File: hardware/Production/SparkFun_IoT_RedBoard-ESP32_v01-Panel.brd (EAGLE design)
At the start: 246.1 x 248.9 mm, 2514 parts, among them J1 5.5x2.1mm Barrel, J101 USB C, J102 USB_SOLDER_PADS, J103 M10NO_SILK, J108 QWIIC_RIGHT_ANGLE, J109 MICRO-SD-PUSH-PUSH-EXT-PIN, J110 5.5x2.1mm Barrel, J117 USB C, J118 USB_SOLDER_PADS, J119 M10NO_SILK, J124 QWIIC_RIGHT_ANGLE, J125 MICRO-SD-PUSH-PUSH-EXT-PIN, J126 5.5x2.1mm Barrel, J13 QWIIC_RIGHT_ANGLE, J133 USB C, J134 USB_SOLDER_PADS, J135 M10NO_SILK, J140 QWIIC_RIGHT_ANGLE, J141 MICRO-SD-PUSH-PUSH-EXT-PIN, J142 5.5x2.1mm Barrel, J149 USB C, J15 MICRO-SD-PUSH-PUSH-EXT-PIN, J150 USB_SOLDER_PADS, J151 M10NO_SILK, J156 QWIIC_RIGHT_ANGLE, J157 MICRO-SD-PUSH-PUSH-EXT-PIN, J158 5.5x2.1mm Barrel, J165 USB C, J166 USB_SOLDER_PADS, J167 M10NO_SILK, J172 QWIIC_RIGHT_ANGLE, J173 MICRO-SD-PUSH-PUSH-EXT-PIN, J174 5.5x2.1mm Barrel, J181 USB C, J182 USB_SOLDER_PADS, J183 M10NO_SILK, J188 QWIIC_RIGHT_ANGLE, J189 MICRO-SD-PUSH-PUSH-EXT-PIN, J190 5.5x2.1mm Barrel, J2 USB C, J21 USB C, J22 USB_SOLDER_PADS, J23 M10NO_SILK, J28 QWIIC_RIGHT_ANGLE, J29 MICRO-SD-PUSH-PUSH-EXT-PIN, J3 USB_SOLDER_PADS, J30 5.5x2.1mm Barrel, J37 USB C, J38 USB_SOLDER_PADS, J39 M10NO_SILK, J44 QWIIC_RIGHT_ANGLE, J45 MICRO-SD-PUSH-PUSH-EXT-PIN, J46 5.5x2.1mm Barrel, J5 M10NO_SILK, J53 USB C, J54 USB_SOLDER_PADS, J55 M10NO_SILK, J60 QWIIC_RIGHT_ANGLE, J61 MICRO-SD-PUSH-PUSH-EXT-PIN, J62 5.5x2.1mm Barrel, J69 USB C, J70 USB_SOLDER_PADS, J71 M10NO_SILK, J76 QWIIC_RIGHT_ANGLE, J77 MICRO-SD-PUSH-PUSH-EXT-PIN, J78 5.5x2.1mm Barrel, J85 USB C, J86 USB_SOLDER_PADS, J87 M10NO_SILK, J92 QWIIC_RIGHT_ANGLE, J93 MICRO-SD-PUSH-PUSH-EXT-PIN, J94 5.5x2.1mm Barrel, Q1 MBT3904DW1T1, Q100 20V/4.2A/52mΩ/1.4W, Q102 20V/4.2A/52mΩ/1.4W, Q104 20V/4.2A/52mΩ/1.4W, Q105 MBT3904DW1T1, Q107 20V/4.2A/52mΩ/1.4W, Q109 20V/4.2A/52mΩ/1.4W, Q11 20V/4.2A/52mΩ/1.4W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

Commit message: Implemented changes suggested by Pete Lewis.
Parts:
- removed LOGO49, LOGO52, LOGO54, LOGO57, LOGO59: QWIIC_LOGO_5MM, SparkFun-Aesthetics:QWIIC_5MM
- removed LOGO50, LOGO55, LOGO60: SFE_LOGO_NAME_FLAME.2_INCH, SparkFun-Aesthetics:SFE_LOGO_NAME_FLAME_.2
- removed LOGO51, LOGO56: SFE_LOGO_NAME.1_INCH, SparkFun-Aesthetics:SFE_LOGO_NAME_.1
- removed LOGO53, LOGO58: OSHW-LOGOMINI, SparkFun-Aesthetics:OSHW-LOGO-MINI
- added U$1177: (no value), output-ESP32:#3#3V#321866
- added U$1178: (no value), output-ESP32:#MEAS#1851
- added U$1179: (no value), output-ESP32:#BYP#35
- added U$1180: (no value), output-ESP32:D#32321863
- added U$1181: (no value), output-ESP32:D#32321862
- added U$1182: (no value), output-ESP32:G32321864
- added U$1183: (no value), output-ESP32:#1849
- added U$1184: (no value), output-ESP32:#1850
- added U$1185: (no value), output-ESP32:#I2C#1855
- added U$1186: (no value), output-ESP32:##ALERT##1852
- added U$1187: (no value), output-ESP32:#TMS#1854
- added U$1188: (no value), output-ESP32:#TCK#1853
- added U$1189, U$1190: (no value), output-ESP32:INPUT_ONLY321867
- added U$1191: (no value), output-ESP32:##ALERT##4#321866
- added U$1192: (no value), output-ESP32:TP1321868
- added U$1193: (no value), SparkFun-Aesthetics:REDBOARD_LOGO
- added U$1194: (no value), output-ESP32:#IOT#132321869
- added U$1195: (no value), output-ESP32:ESP32321856
- added U$1196: (no value), output-ESP32:#IOT#132321874
- added U$1197: (no value), output-ESP32:MADE_IN32321857
- added U$1198: (no value), output-ESP32:THE_USA32321858
- added U$1199: (no value), output-ESP32:7#15V32321861
- added U$1200: (no value), output-ESP32:3#3V_LOGIC_SHIELDS_ONLY132321876
- LOGO10, LOGO30: value SFE_LOGO_NAME_FLAME.2_INCH -> QWIIC_LOGO_5MM; device SparkFun-Aesthetics:SFE_LOGO_NAME_FLAME_.2 -> SparkFun-Aesthetics:QWIIC_5MM
- LOGO11, LOGO31: value SFE_LOGO_NAME.1_INCH -> OSHW-LOGOMINI; device SparkFun-Aesthetics:SFE_LOGO_NAME_.1 -> SparkFun-Aesthetics:OSHW-LOGO-MINI
- LOGO12, LOGO24, LOGO32, LOGO44: value QWIIC_LOGO_5MM -> SFE_LOGO_NAME_FLAME.2_INCH; device SparkFun-Aesthetics:QWIIC_5MM -> SparkFun-Aesthetics:SFE_LOGO_NAME_FLAME_.2
- LOGO13, LOGO33: value OSHW-LOGOMINI -> SFE_LOGO_NAME.1_INCH; device SparkFun-Aesthetics:OSHW-LOGO-MINI -> SparkFun-Aesthetics:SFE_LOGO_NAME_.1
- LOGO15, LOGO35: value SFE_LOGO_NAME_FLAME.2_INCH -> OSHW-LOGOMINI; device SparkFun-Aesthetics:SFE_LOGO_NAME_FLAME_.2 -> SparkFun-Aesthetics:OSHW-LOGO-MINI
- LOGO16, LOGO36: value SFE_LOGO_NAME.1_INCH -> SFE_LOGO_NAME_FLAME.2_INCH; device SparkFun-Aesthetics:SFE_LOGO_NAME_.1 -> SparkFun-Aesthetics:SFE_LOGO_NAME_FLAME_.2
- LOGO17, LOGO29, LOGO37, LOGO4, LOGO9: value QWIIC_LOGO_5MM -> SFE_LOGO_NAME.1_INCH; device SparkFun-Aesthetics:QWIIC_5MM -> SparkFun-Aesthetics:SFE_LOGO_NAME_.1
- LOGO18, LOGO38: value OSHW-LOGOMINI -> QWIIC_LOGO_5MM; device SparkFun-Aesthetics:OSHW-LOGO-MINI -> SparkFun-Aesthetics:QWIIC_5MM
- LOGO19, LOGO27, LOGO39, LOGO47, LOGO7: value QWIIC_LOGO_5MM -> OSHW-LOGOMINI; device SparkFun-Aesthetics:QWIIC_5MM -> SparkFun-Aesthetics:OSHW-LOGO-MINI
- LOGO25, LOGO45: value SFE_LOGO_NAME_FLAME.2_INCH -> SFE_LOGO_NAME.1_INCH; device SparkFun-Aesthetics:SFE_LOGO_NAME_FLAME_.2 -> SparkFun-Aesthetics:SFE_LOGO_NAME_.1
- LOGO26, LOGO46, LOGO5: value SFE_LOGO_NAME.1_INCH -> QWIIC_LOGO_5MM; device SparkFun-Aesthetics:SFE_LOGO_NAME_.1 -> SparkFun-Aesthetics:QWIIC_5MM
- LOGO28, LOGO48, LOGO8: value OSHW-LOGOMINI -> SFE_LOGO_NAME_FLAME.2_INCH; device SparkFun-Aesthetics:OSHW-LOGO-MINI -> SparkFun-Aesthetics:SFE_LOGO_NAME_FLAME_.2
- U$1000: device output-ESP32:#14#14 -> output-ESP32:3#3V_LOGIC_SHIELDS_ONLY132321876
- U$1001: device output-ESP32:#13#5 -> output-ESP32:V323252
- U$1002: device output-ESP32:#4#2 -> output-ESP32:#SCL#34
- U$1003: device output-ESP32:#TX#O#0 -> output-ESP32:#SDA#33
- U$1004: device output-ESP32:#RX#I#1 -> output-ESP32:#3#3V#33
- U$1005: device output-ESP32:#RESET#1842 -> output-ESP32:#GND#32
- U$1006: device output-ESP32:#BOOT#1841 -> output-ESP32:#SCK#31
- U$1007: device output-ESP32:#JTAG#1847 -> output-ESP32:#POCI#30
- U$1008: device output-ESP32:#A0#1843 -> output-ESP32:#PICO#29
- U$1009: device output-ESP32:#A3#1843 -> output-ESP32:1836
- U$101, U$199: device output-ESP32:#SDA#33 -> output-ESP32:7#15V32321861
- U$1010: device output-ESP32:#A6#1843 -> output-ESP32:##CS##28
- U$1011: device output-ESP32:#A7#1843 -> output-ESP32:#27#27
- U$1012: device output-ESP32:#A4#1843 -> output-ESP32:#26#26
- U$1013: device output-ESP32:#A5#1843 -> output-ESP32:TX1838
- U$1014: device output-ESP32:#VIN#1843 -> output-ESP32:RX1839
- U$1015: device output-ESP32:#GND#1844 -> output-ESP32:PWR1837
- U$1016: device output-ESP32:#GND#1844 -> output-ESP32:CHG1840
- U$1017: device output-ESP32:#5V#1845 -> output-ESP32:#25#18
- U$1018: device output-ESP32:#3#3V#1845 -> output-ESP32:#17#17
- U$1019: device output-ESP32:##RST##1845 -> output-ESP32:#16#15
- U$102: device output-ESP32:#3#3V#33 -> output-ESP32:#SDA#33
- U$1020: device output-ESP32:#REF#1846 -> output-ESP32:#14#14
- U$1021: device output-ESP32:#MEAS#1851 -> output-ESP32:#13#5
- U$1022: device output-ESP32:#1849 -> output-ESP32:#4#2
- U$1023: device output-ESP32:#1850 -> output-ESP32:#TX#O#0
- U$1024: device output-ESP32:#BATT#1848 -> output-ESP32:#RX#I#1
- U$1025, U$125: device output-ESP32:#JTAG#1847 -> output-ESP32:#RESET#1842
- U$1026: device output-ESP32:ESP321855 -> output-ESP32:#BOOT#1841
- U$1027, U$145: device output-ESP32:7#15V32321861 -> output-ESP32:#JTAG#1847
- U$1028: device output-ESP32:#39#A3#321862 -> output-ESP32:#A0#1843
- U$1029: device output-ESP32:#36#A0#321862 -> output-ESP32:#A3#1843
- U$103: device output-ESP32:#GND#32 -> output-ESP32:3#3V_LOGIC_SHIELDS_ONLY132321876
- U$1030: device output-ESP32:#34#A6#32321865 -> output-ESP32:#A6#1843
- U$1031: device output-ESP32:#35#A7#321862 -> output-ESP32:#A7#1843
- U$1032: device output-ESP32:#32#A4#32321865 -> output-ESP32:#A4#1843
- U$1033: device output-ESP32:#34#A6#321862 -> output-ESP32:#A5#1843
- U$1034: device output-ESP32:#VIN#321862 -> output-ESP32:#VIN#1843
- U$1035, U$1136: device output-ESP32:#GND#321863 -> output-ESP32:#GND#1844
- U$1036: device output-ESP32:#5V#321864 -> output-ESP32:#GND#1844
- U$1037: device output-ESP32:#3#3V#321864 -> output-ESP32:#5V#1845
- U$1038: device output-ESP32:#GND#321863 -> output-ESP32:#3#3V#1845
- U$1039: device output-ESP32:##RESET##321864 -> output-ESP32:##RST##1845
- U$104: device output-ESP32:#SCK#31 -> output-ESP32:#3#3V#33
- U$1040: device output-ESP32:#IOREF#321865 -> output-ESP32:#REF#1846
- U$1041: device output-ESP32:#3#RX#I#32321869 -> output-ESP32:#MEAS#1851
- U$1042: device output-ESP32:#1#TX#O#32321869 -> output-ESP32:#1849
- U$1043: device output-ESP32:#13#TCK#32321869 -> output-ESP32:#1850
- U$1044: device output-ESP32:#14#TMS#32321869 -> output-ESP32:#BATT#1848
- U$1045: device output-ESP32:#16#32321869 -> output-ESP32:#JTAG#1847
- U$1046: device output-ESP32:#17#32321869 -> output-ESP32:ESP321855
- U$1047: device output-ESP32:#25#32321869 -> output-ESP32:7#15V32321861
- U$1048: device output-ESP32:#26#32321869 -> output-ESP32:#39#A3#321862
- U$1049: device output-ESP32:#5##CS##32321869 -> output-ESP32:#36#A0#321862
- U$105: device output-ESP32:#POCI#30 -> output-ESP32:#GND#32
- U$1050: device output-ESP32:#23#PICO#321866 -> output-ESP32:#34#A6#32321865
- U$1051: device output-ESP32:#19#POCI#321866 -> output-ESP32:#35#A7#321862
- U$1052: device output-ESP32:#18#SCK#32321869 -> output-ESP32:#32#A4#32321865
- U$1053: device output-ESP32:#21#SDA#32321869 -> output-ESP32:#34#A6#321862
- U$1054: device output-ESP32:#22#SCL#32321869 -> output-ESP32:#VIN#321862
- U$1055: device output-ESP32:#27#32321869 -> output-ESP32:#GND#321863
- U$1056: device output-ESP32:#GND#321866 -> output-ESP32:#5V#321864
- U$1057: device output-ESP32:#3#3V#321866 -> output-ESP32:#3#3V#321864
- U$1058: device output-ESP32:#MEAS#1851 -> output-ESP32:#GND#321863
- U$1059: device output-ESP32:#BYP#35 -> output-ESP32:##RESET##321864
- U$106: device output-ESP32:#PICO#29 -> output-ESP32:#SCK#31
- U$1060: device output-ESP32:D#32321863 -> output-ESP32:#IOREF#321865
- U$1061: device output-ESP32:D#32321862 -> output-ESP32:#3#RX#I#32321869
- U$1062: device output-ESP32:G32321864 -> output-ESP32:#1#TX#O#32321869
- U$1063: device output-ESP32:#1849 -> output-ESP32:#13#TCK#32321869
- U$1064: device output-ESP32:#1850 -> output-ESP32:#14#TMS#32321869
- U$1065: device output-ESP32:#I2C#1855 -> output-ESP32:#16#32321869
- U$1066: device output-ESP32:##ALERT##1852 -> output-ESP32:#17#32321869
- U$1067: device output-ESP32:#TMS#1854 -> output-ESP32:#25#32321869
- U$1068: device output-ESP32:#TCK#1853 -> output-ESP32:#26#32321869
- U$1069: device output-ESP32:INPUT_ONLY321867 -> output-ESP32:#5##CS##32321869
- U$107: device output-ESP32:1836 -> output-ESP32:#POCI#30
- U$1070: device output-ESP32:INPUT_ONLY321867 -> output-ESP32:#23#PICO#321866
- U$1071: device output-ESP32:##ALERT##4#321866 -> output-ESP32:#19#POCI#321866
- U$1072: device output-ESP32:TP1321868 -> output-ESP32:#18#SCK#32321869
- U$1073: device SparkFun-Aesthetics:REDBOARD_LOGO -> output-ESP32:#21#SDA#32321869
- U$1074: device output-ESP32:#IOT#132321869 -> output-ESP32:#22#SCL#32321869
- U$1075: device output-ESP32:ESP32321856 -> output-ESP32:#27#32321869
- U$1076: device output-ESP32:#IOT#132321874 -> output-ESP32:#GND#321866
- U$1077: device output-ESP32:MADE_IN32321857 -> output-ESP32:#3#3V#321866
- U$1078: device output-ESP32:THE_USA32321858 -> output-ESP32:#MEAS#1851
- U$1079: device output-ESP32:V323252 -> output-ESP32:#BYP#35
- U$108: device output-ESP32:##CS##28 -> output-ESP32:#PICO#29
- U$1080: device output-ESP32:#SCL#34 -> output-ESP32:D#32321863
- U$1081: device output-ESP32:#SDA#33 -> output-ESP32:D#32321862
- U$1082: device output-ESP32:#3#3V#33 -> output-ESP32:G32321864
- U$1083: device output-ESP32:#GND#32 -> output-ESP32:#1849
- U$1084: device output-ESP32:#SCK#31 -> output-ESP32:#1850
- U$1085: device output-ESP32:#POCI#30 -> output-ESP32:#I2C#1855
- U$1086: device output-ESP32:#PICO#29 -> output-ESP32:##ALERT##1852
- U$1087: device output-ESP32:1836 -> output-ESP32:#TMS#1854
- U$1088: device output-ESP32:##CS##28 -> output-ESP32:#TCK#1853
- U$1089: device output-ESP32:#27#27 -> output-ESP32:INPUT_ONLY321867
- U$109: device output-ESP32:#27#27 -> output-ESP32:1836
- U$1090: device output-ESP32:#26#26 -> output-ESP32:INPUT_ONLY321867
- U$1091: device output-ESP32:TX1838 -> output-ESP32:##ALERT##4#321866
- U$1092: device output-ESP32:RX1839 -> output-ESP32:TP1321868
- U$1093: device output-ESP32:PWR1837 -> SparkFun-Aesthetics:REDBOARD_LOGO
- U$1094: device output-ESP32:CHG1840 -> output-ESP32:#IOT#132321869
- U$1095: device output-ESP32:#25#18 -> output-ESP32:ESP32321856
- U$1096: device output-ESP32:#17#17 -> output-ESP32:#IOT#132321874
- U$1097: device output-ESP32:#16#15 -> output-ESP32:MADE_IN32321857
- U$1098: device output-ESP32:#14#14 -> output-ESP32:THE_USA32321858
- U$1099: device output-ESP32:#13#5 -> output-ESP32:7#15V32321861
- U$110: device output-ESP32:#26#26 -> output-ESP32:##CS##28
- U$1100: device output-ESP32:#4#2 -> output-ESP32:3#3V_LOGIC_SHIELDS_ONLY132321876
- U$1101: device output-ESP32:#TX#O#0 -> output-ESP32:V323252
- U$1102: device output-ESP32:#RX#I#1 -> output-ESP32:#SCL#34
- U$1103: device output-ESP32:#RESET#1842 -> output-ESP32:#SDA#33
- U$1104: device output-ESP32:#BOOT#1841 -> output-ESP32:#3#3V#33
- U$1105: device output-ESP32:#JTAG#1847 -> output-ESP32:#GND#32
- U$1106: device output-ESP32:#A0#1843 -> output-ESP32:#SCK#31
- U$1107: device output-ESP32:#A3#1843 -> output-ESP32:#POCI#30
- U$1108: device output-ESP32:#A6#1843 -> output-ESP32:#PICO#29
- U$1109: device output-ESP32:#A7#1843 -> output-ESP32:1836
- U$111: device output-ESP32:TX1838 -> output-ESP32:#27#27
- U$1110: device output-ESP32:#A4#1843 -> output-ESP32:##CS##28
- U$1111: device output-ESP32:#A5#1843 -> output-ESP32:#27#27
- U$1112: device output-ESP32:#VIN#1843 -> output-ESP32:#26#26
- U$1113: device output-ESP32:#GND#1844 -> output-ESP32:TX1838
- U$1114: device output-ESP32:#GND#1844 -> output-ESP32:RX1839
- U$1115: device output-ESP32:#5V#1845 -> output-ESP32:PWR1837
- U$1116: device output-ESP32:#3#3V#1845 -> output-ESP32:CHG1840
- U$1117: device output-ESP32:##RST##1845 -> output-ESP32:#25#18
- U$1118: device output-ESP32:#REF#1846 -> output-ESP32:#17#17
- U$1119: device output-ESP32:#MEAS#1851 -> output-ESP32:#16#15
- U$112: device output-ESP32:RX1839 -> output-ESP32:#26#26
- U$1120: device output-ESP32:#1849 -> output-ESP32:#14#14
- U$1121: device output-ESP32:#1850 -> output-ESP32:#13#5
- U$1122: device output-ESP32:#BATT#1848 -> output-ESP32:#4#2
- U$1123, U$223: device output-ESP32:#JTAG#1847 -> output-ESP32:#TX#O#0
- U$1124: device output-ESP32:ESP321855 -> output-ESP32:#RX#I#1
- U$1125: device output-ESP32:7#15V32321861 -> output-ESP32:#RESET#1842
- U$1126: device output-ESP32:#39#A3#321862 -> output-ESP32:#BOOT#1841
- U$1127, U$245: device output-ESP32:#36#A0#321862 -> output-ESP32:#JTAG#1847
- U$1128: device output-ESP32:#34#A6#32321865 -> output-ESP32:#A0#1843
- U$1129: device output-ESP32:#35#A7#321862 -> output-ESP32:#A3#1843
- U$113: device output-ESP32:PWR1837 -> output-ESP32:TX1838
- U$1130: device output-ESP32:#32#A4#32321865 -> output-ESP32:#A6#1843
- U$1131: device output-ESP32:#34#A6#321862 -> output-ESP32:#A7#1843
- U$1132: device output-ESP32:#VIN#321862 -> output-ESP32:#A4#1843
- U$1133: device output-ESP32:#GND#321863 -> output-ESP32:#A5#1843
- U$1134: device output-ESP32:#5V#321864 -> output-ESP32:#VIN#1843
- U$1135: device output-ESP32:#3#3V#321864 -> output-ESP32:#GND#1844
- U$1137: device output-ESP32:##RESET##321864 -> output-ESP32:#5V#1845
- U$1138: device output-ESP32:#IOREF#321865 -> output-ESP32:#3#3V#1845
- U$1139: device output-ESP32:#3#RX#I#32321869 -> output-ESP32:##RST##1845
- U$114: device output-ESP32:CHG1840 -> output-ESP32:RX1839
- U$1140: device output-ESP32:#1#TX#O#32321869 -> output-ESP32:#REF#1846
- U$1141: device output-ESP32:#13#TCK#32321869 -> output-ESP32:#MEAS#1851
- U$1142: device output-ESP32:#14#TMS#32321869 -> output-ESP32:#1849
- U$1143: device output-ESP32:#16#32321869 -> output-ESP32:#1850
- U$1144: device output-ESP32:#17#32321869 -> output-ESP32:#BATT#1848
- U$1145: device output-ESP32:#25#32321869 -> output-ESP32:#JTAG#1847
- U$1146: device output-ESP32:#26#32321869 -> output-ESP32:ESP321855
- U$1147: device output-ESP32:#5##CS##32321869 -> output-ESP32:7#15V32321861
- U$1148: device output-ESP32:#23#PICO#321866 -> output-ESP32:#39#A3#321862
- U$1149: device output-ESP32:#19#POCI#321866 -> output-ESP32:#36#A0#321862
- U$115: device output-ESP32:#25#18 -> output-ESP32:PWR1837
- U$1150: device output-ESP32:#18#SCK#32321869 -> output-ESP32:#34#A6#32321865
- U$1151: device output-ESP32:#21#SDA#32321869 -> output-ESP32:#35#A7#321862
- U$1152: device output-ESP32:#22#SCL#32321869 -> output-ESP32:#32#A4#32321865
- U$1153: device output-ESP32:#27#32321869 -> output-ESP32:#34#A6#321862
- U$1154: device output-ESP32:#GND#321866 -> output-ESP32:#VIN#321862
- U$1155: device output-ESP32:#3#3V#321866 -> output-ESP32:#GND#321863
- U$1156: device output-ESP32:#MEAS#1851 -> output-ESP32:#5V#321864
- U$1157: device output-ESP32:#BYP#35 -> output-ESP32:#3#3V#321864
- U$1158: device output-ESP32:D#32321863 -> output-ESP32:#GND#321863
- U$1159: device output-ESP32:D#32321862 -> output-ESP32:##RESET##321864
- U$116: device output-ESP32:#17#17 -> output-ESP32:CHG1840
- U$1160: device output-ESP32:G32321864 -> output-ESP32:#IOREF#321865
- U$1161: device output-ESP32:#1849 -> output-ESP32:#3#RX#I#32321869
- U$1162: device output-ESP32:#1850 -> output-ESP32:#1#TX#O#32321869
- U$1163: device output-ESP32:#I2C#1855 -> output-ESP32:#13#TCK#32321869
- U$1164: device output-ESP32:##ALERT##1852 -> output-ESP32:#14#TMS#32321869
- U$1165: device output-ESP32:#TMS#1854 -> output-ESP32:#16#32321869
- U$1166: device output-ESP32:#TCK#1853 -> output-ESP32:#17#32321869
- U$1167: device output-ESP32:INPUT_ONLY321867 -> output-ESP32:#25#32321869
- U$1168: device output-ESP32:INPUT_ONLY321867 -> output-ESP32:#26#32321869
- U$1169: device output-ESP32:##ALERT##4#321866 -> output-ESP32:#5##CS##32321869
- U$117: device output-ESP32:#16#15 -> output-ESP32:#25#18
- U$1170: device output-ESP32:TP1321868 -> output-ESP32:#23#PICO#321866
- U$1171: device SparkFun-Aesthetics:REDBOARD_LOGO -> output-ESP32:#19#POCI#321866
- U$1172: device output-ESP32:#IOT#132321869 -> output-ESP32:#18#SCK#32321869
- U$1173: device output-ESP32:ESP32321856 -> output-ESP32:#21#SDA#32321869
- U$1174: device output-ESP32:#IOT#132321874 -> output-ESP32:#22#SCL#32321869
- U$1175: device output-ESP32:MADE_IN32321857 -> output-ESP32:#27#32321869
- U$1176: device output-ESP32:THE_USA32321858 -> output-ESP32:#GND#321866
- U$118: device output-ESP32:#14#14 -> output-ESP32:#17#17
- U$119: device output-ESP32:#13#5 -> output-ESP32:#16#15
- U$120: device output-ESP32:#4#2 -> output-ESP32:#14#14
- U$121: device output-ESP32:#TX#O#0 -> output-ESP32:#13#5
- U$122: device output-ESP32:#RX#I#1 -> output-ESP32:#4#2
- U$123: device output-ESP32:#RESET#1842 -> output-ESP32:#TX#O#0
- U$124: device output-ESP32:#BOOT#1841 -> output-ESP32:#RX#I#1
- U$126: device output-ESP32:#A0#1843 -> output-ESP32:#BOOT#1841
- U$127: device output-ESP32:#A3#1843 -> output-ESP32:#JTAG#1847
- U$128: device output-ESP32:#A6#1843 -> output-ESP32:#A0#1843
- U$129: device output-ESP32:#A7#1843 -> output-ESP32:#A3#1843
- U$130: device output-ESP32:#A4#1843 -> output-ESP32:#A6#1843
- U$131: device output-ESP32:#A5#1843 -> output-ESP32:#A7#1843
- U$132: device output-ESP32:#VIN#1843 -> output-ESP32:#A4#1843
- U$133: device output-ESP32:#GND#1844 -> output-ESP32:#A5#1843
- U$134: device output-ESP32:#GND#1844 -> output-ESP32:#VIN#1843
- U$135: device output-ESP32:#5V#1845 -> output-ESP32:#GND#1844
- U$136: device output-ESP32:#3#3V#1845 -> output-ESP32:#GND#1844
- U$137: device output-ESP32:##RST##1845 -> output-ESP32:#5V#1845
- U$138: device output-ESP32:#REF#1846 -> output-ESP32:#3#3V#1845
- U$139: device output-ESP32:#MEAS#1851 -> output-ESP32:##RST##1845
- U$140: device output-ESP32:#1849 -> output-ESP32:#REF#1846
- U$141, U$378: device output-ESP32:#1850 -> output-ESP32:#MEAS#1851
- U$142: device output-ESP32:#BATT#1848 -> output-ESP32:#1849
- U$143: device output-ESP32:#JTAG#1847 -> output-ESP32:#1850
- U$144: device output-ESP32:ESP321855 -> output-ESP32:#BATT#1848
- U$146: device output-ESP32:#39#A3#321862 -> output-ESP32:ESP321855
- U$147: device output-ESP32:#36#A0#321862 -> output-ESP32:7#15V32321861
- U$148: device output-ESP32:#34#A6#32321865 -> output-ESP32:#39#A3#321862
- U$149: device output-ESP32:#35#A7#321862 -> output-ESP32:#36#A0#321862
- U$150: device output-ESP32:#32#A4#32321865 -> output-ESP32:#34#A6#32321865
- U$151: device output-ESP32:#34#A6#321862 -> output-ESP32:#35#A7#321862
- U$152: device output-ESP32:#VIN#321862 -> output-ESP32:#32#A4#32321865
- U$153: device output-ESP32:#GND#321863 -> output-ESP32:#34#A6#321862
- U$154: device output-ESP32:#5V#321864 -> output-ESP32:#VIN#321862
- U$155: device output-ESP32:#3#3V#321864 -> output-ESP32:#GND#321863
- U$156: device output-ESP32:#GND#321863 -> output-ESP32:#5V#321864
- U$157: device output-ESP32:##RESET##321864 -> output-ESP32:#3#3V#321864
- U$158: device output-ESP32:#IOREF#321865 -> output-ESP32:#GND#321863
- U$159: device output-ESP32:#3#RX#I#32321869 -> output-ESP32:##RESET##321864
- U$160: device output-ESP32:#1#TX#O#32321869 -> output-ESP32:#IOREF#321865
- U$161: device output-ESP32:#13#TCK#32321869 -> output-ESP32:#3#RX#I#32321869
- U$162: device output-ESP32:#14#TMS#32321869 -> output-ESP32:#1#TX#O#32321869
- U$163: device output-ESP32:#16#32321869 -> output-ESP32:#13#TCK#32321869
- U$164: device output-ESP32:#17#32321869 -> output-ESP32:#14#TMS#32321869
- U$165: device output-ESP32:#25#32321869 -> output-ESP32:#16#32321869
- U$166: device output-ESP32:#26#32321869 -> output-ESP32:#17#32321869
- U$167: device output-ESP32:#5##CS##32321869 -> output-ESP32:#25#32321869
- U$168: device output-ESP32:#23#PICO#321866 -> output-ESP32:#26#32321869
- U$169: device output-ESP32:#19#POCI#321866 -> output-ESP32:#5##CS##32321869
- U$170: device output-ESP32:#18#SCK#32321869 -> output-ESP32:#23#PICO#321866
- U$171: device output-ESP32:#21#SDA#32321869 -> output-ESP32:#19#POCI#321866
- U$172: device output-ESP32:#22#SCL#32321869 -> output-ESP32:#18#SCK#32321869
- U$173: device output-ESP32:#27#32321869 -> output-ESP32:#21#SDA#32321869
- U$174: device output-ESP32:#GND#321866 -> output-ESP32:#22#SCL#32321869
- U$175: device output-ESP32:#3#3V#321866 -> output-ESP32:#27#32321869
- U$176: device output-ESP32:#MEAS#1851 -> output-ESP32:#GND#321866
- U$177: device output-ESP32:#BYP#35 -> output-ESP32:#3#3V#321866
- U$178: device output-ESP32:D#32321863 -> output-ESP32:#MEAS#1851
- U$179: device output-ESP32:D#32321862 -> output-ESP32:#BYP#35
- U$180: device output-ESP32:G32321864 -> output-ESP32:D#32321863
- U$181: device output-ESP32:#1849 -> output-ESP32:D#32321862
- U$182: device output-ESP32:#1850 -> output-ESP32:G32321864
- U$183: device output-ESP32:#I2C#1855 -> output-ESP32:#1849
- U$184: device output-ESP32:##ALERT##1852 -> output-ESP32:#1850
- U$185: device output-ESP32:#TMS#1854 -> output-ESP32:#I2C#1855
- U$186: device output-ESP32:#TCK#1853 -> output-ESP32:##ALERT##1852
- U$187: device output-ESP32:INPUT_ONLY321867 -> output-ESP32:#TMS#1854
- U$188: device output-ESP32:INPUT_ONLY321867 -> output-ESP32:#TCK#1853
- U$189: device output-ESP32:##ALERT##4#321866 -> output-ESP32:INPUT_ONLY321867
- U$190: device output-ESP32:TP1321868 -> output-ESP32:INPUT_ONLY321867
- U$191: device SparkFun-Aesthetics:REDBOARD_LOGO -> output-ESP32:##ALERT##4#321866
- U$192: device output-ESP32:#IOT#132321869 -> output-ESP32:TP1321868
- U$193: device output-ESP32:ESP32321856 -> SparkFun-Aesthetics:REDBOARD_LOGO
- U$194: device output-ESP32:#IOT#132321874 -> output-ESP32:#IOT#132321869
- U$195: device output-ESP32:MADE_IN32321857 -> output-ESP32:ESP32321856
- U$196: device output-ESP32:THE_USA32321858 -> output-ESP32:#IOT#132321874
- U$197: device output-ESP32:V323252 -> output-ESP32:MADE_IN32321857
- U$198: device output-ESP32:#SCL#34 -> output-ESP32:THE_USA32321858
- U$200: device output-ESP32:#3#3V#33 -> output-ESP32:3#3V_LOGIC_SHIELDS_ONLY132321876
- U$201: device output-ESP32:#GND#32 -> output-ESP32:V323252
- U$202: device output-ESP32:#SCK#31 -> output-ESP32:#SCL#34
- U$203: device output-ESP32:#POCI#30 -> output-ESP32:#SDA#33
- U$204: device output-ESP32:#PICO#29 -> output-ESP32:#3#3V#33
- U$205: device output-ESP32:1836 -> output-ESP32:#GND#32
- U$206: device output-ESP32:##CS##28 -> output-ESP32:#SCK#31
- U$207: device output-ESP32:#27#27 -> output-ESP32:#POCI#30
- U$208: device output-ESP32:#26#26 -> output-ESP32:#PICO#29
- U$209: device output-ESP32:TX1838 -> output-ESP32:1836
- U$210: device output-ESP32:RX1839 -> output-ESP32:##CS##28
- U$211: device output-ESP32:PWR1837 -> output-ESP32:#27#27
- U$212: device output-ESP32:CHG1840 -> output-ESP32:#26#26
- U$213: device output-ESP32:#25#18 -> output-ESP32:TX1838
- U$214: device output-ESP32:#17#17 -> output-ESP32:RX1839
- U$215: device output-ESP32:#16#15 -> output-ESP32:PWR1837
- U$216: device output-ESP32:#14#14 -> output-ESP32:CHG1840
- U$217: device output-ESP32:#13#5 -> output-ESP32:#25#18
- U$218: device output-ESP32:#4#2 -> output-ESP32:#17#17
- U$219: device output-ESP32:#TX#O#0 -> output-ESP32:#16#15
- U$220: device output-ESP32:#RX#I#1 -> output-ESP32:#14#14
- U$221: device output-ESP32:#RESET#1842 -> output-ESP32:#13#5
- U$222: device output-ESP32:#BOOT#1841 -> output-ESP32:#4#2
- U$224: device output-ESP32:#A0#1843 -> output-ESP32:#RX#I#1
- U$225: device output-ESP32:#A3#1843 -> output-ESP32:#RESET#1842
- U$226: device output-ESP32:#A6#1843 -> output-ESP32:#BOOT#1841
- U$227: device output-ESP32:#A7#1843 -> output-ESP32:#JTAG#1847
- U$228: device output-ESP32:#A4#1843 -> output-ESP32:#A0#1843
- U$229: device output-ESP32:#A5#1843 -> output-ESP32:#A3#1843
- U$230: device output-ESP32:#VIN#1843 -> output-ESP32:#A6#1843
- U$231: device output-ESP32:#GND#1844 -> output-ESP32:#A7#1843
- U$232: device output-ESP32:#GND#1844 -> output-ESP32:#A4#1843
- U$233: device output-ESP32:#5V#1845 -> output-ESP32:#A5#1843
- U$234: device output-ESP32:#3#3V#1845 -> output-ESP32:#VIN#1843
- U$235: device output-ESP32:##RST##1845 -> output-ESP32:#GND#1844
- U$236: device output-ESP32:#REF#1846 -> output-ESP32:#GND#1844
- U$237: device output-ESP32:#MEAS#1851 -> output-ESP32:#5V#1845
- U$238: device output-ESP32:#1849 -> output-ESP32:#3#3V#1845
- U$239: device output-ESP32:#1850 -> output-ESP32:##RST##1845
- U$240: device output-ESP32:#BATT#1848 -> output-ESP32:#REF#1846
- U$241: device output-ESP32:#JTAG#1847 -> output-ESP32:#MEAS#1851
- U$242: device output-ESP32:ESP321855 -> output-ESP32:#1849
- U$243: device output-ESP32:7#15V32321861 -> output-ESP32:#1850
- U$244: device output-ESP32:#39#A3#321862 -> output-ESP32:#BATT#1848
- U$246: device output-ESP32:#34#A6#32321865 -> output-ESP32:ESP321855
- U$247: device output-ESP32:#35#A7#321862 -> output-ESP32:7#15V32321861
- U$248: device output-ESP32:#32#A4#32321865 -> output-ESP32:#39#A3#321862
- U$249: device output-ESP32:#34#A6#321862 -> output-ESP32:#36#A0#321862
- U$250: device output-ESP32:#VIN#321862 -> output-ESP32:#34#A6#32321865
- U$251: device output-ESP32:#GND#321863 -> output-ESP32:#35#A7#321862
- U$252: device output-ESP32:#5V#321864 -> output-ESP32:#32#A4#32321865
- U$253: device output-ESP32:#3#3V#321864 -> output-ESP32:#34#A6#321862
- U$254: device output-ESP32:#GND#321863 -> output-ESP32:#VIN#321862
- U$255: device output-ESP32:##RESET##321864 -> output-ESP32:#GND#321863
- U$256: device output-ESP32:#IOREF#321865 -> output-ESP32:#5V#321864
- U$257: device output-ESP32:#3#RX#I#32321869 -> output-ESP32:#3#3V#321864
- U$258: device output-ESP32:#1#TX#O#32321869 -> output-ESP32:#GND#321863
- U$259: device output-ESP32:#13#TCK#32321869 -> output-ESP32:##RESET##321864
- U$260: device output-ESP32:#14#TMS#32321869 -> output-ESP32:#IOREF#321865
- U$261: device output-ESP32:#16#32321869 -> output-ESP32:#3#RX#I#32321869
- U$262: device output-ESP32:#17#32321869 -> output-ESP32:#1#TX#O#32321869
- U$263: device output-ESP32:#25#32321869 -> output-ESP32:#13#TCK#32321869
- U$264: device output-ESP32:#26#32321869 -> output-ESP32:#14#TMS#32321869
- U$265: device output-ESP32:#5##CS##32321869 -> output-ESP32:#16#32321869
- U$266: device output-ESP32:#23#PICO#321866 -> output-ESP32:#17#32321869
- U$267: device output-ESP32:#19#POCI#321866 -> output-ESP32:#25#32321869
- U$268: device output-ESP32:#18#SCK#32321869 -> output-ESP32:#26#32321869
- U$269: device output-ESP32:#21#SDA#32321869 -> output-ESP32:#5##CS##32321869
- U$270: device output-ESP32:#22#SCL#32321869 -> output-ESP32:#23#PICO#321866
- U$271: device output-ESP32:#27#32321869 -> output-ESP32:#19#POCI#321866
- U$272: device output-ESP32:#GND#321866 -> output-ESP32:#18#SCK#32321869
- U$273: device output-ESP32:#3#3V#321866 -> output-ESP32:#21#SDA#32321869
- U$274: device output-ESP32:#MEAS#1851 -> output-ESP32:#22#SCL#32321869
- U$275: device output-ESP32:#BYP#35 -> output-ESP32:#27#32321869
- U$276: device output-ESP32:D#32321863 -> output-ESP32:#GND#321866
- U$277: device output-ESP32:D#32321862 -> output-ESP32:#3#3V#321866
- U$278: device output-ESP32:G32321864 -> output-ESP32:#MEAS#1851
- U$279: device output-ESP32:#1849 -> output-ESP32:#BYP#35
- U$280: device output-ESP32:#1850 -> output-ESP32:D#32321863
- U$281: device output-ESP32:#I2C#1855 -> output-ESP32:D#32321862
- U$282: device output-ESP32:##ALERT##1852 -> output-ESP32:G32321864
- U$283: device output-ESP32:#TMS#1854 -> output-ESP32:#1849
- U$284: device output-ESP32:#TCK#1853 -> output-ESP32:#1850
- U$285: device output-ESP32:INPUT_ONLY321867 -> output-ESP32:#I2C#1855
- U$286: device output-ESP32:INPUT_ONLY321867 -> output-ESP32:##ALERT##1852
- U$287: device output-ESP32:##ALERT##4#321866 -> output-ESP32:#TMS#1854
- U$288: device output-ESP32:TP1321868 -> output-ESP32:#TCK#1853
- U$289: device SparkFun-Aesthetics:REDBOARD_LOGO -> output-ESP32:INPUT_ONLY321867
- U$290: device output-ESP32:#IOT#132321869 -> output-ESP32:INPUT_ONLY321867
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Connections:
- net VUSB renamed VBUS
- net VUSB1 renamed VBUS1
- net VUSB10 renamed VBUS10
- net VUSB11 renamed VBUS11
- net VUSB2 renamed VBUS2
- net VUSB3 renamed VBUS3
- net VUSB4 renamed VBUS4
- net VUSB5 renamed VBUS5
- net VUSB6 renamed VBUS6
- net VUSB7 renamed VBUS7
- net VUSB8 renamed VBUS8
- net VUSB9 renamed VBUS9
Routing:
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
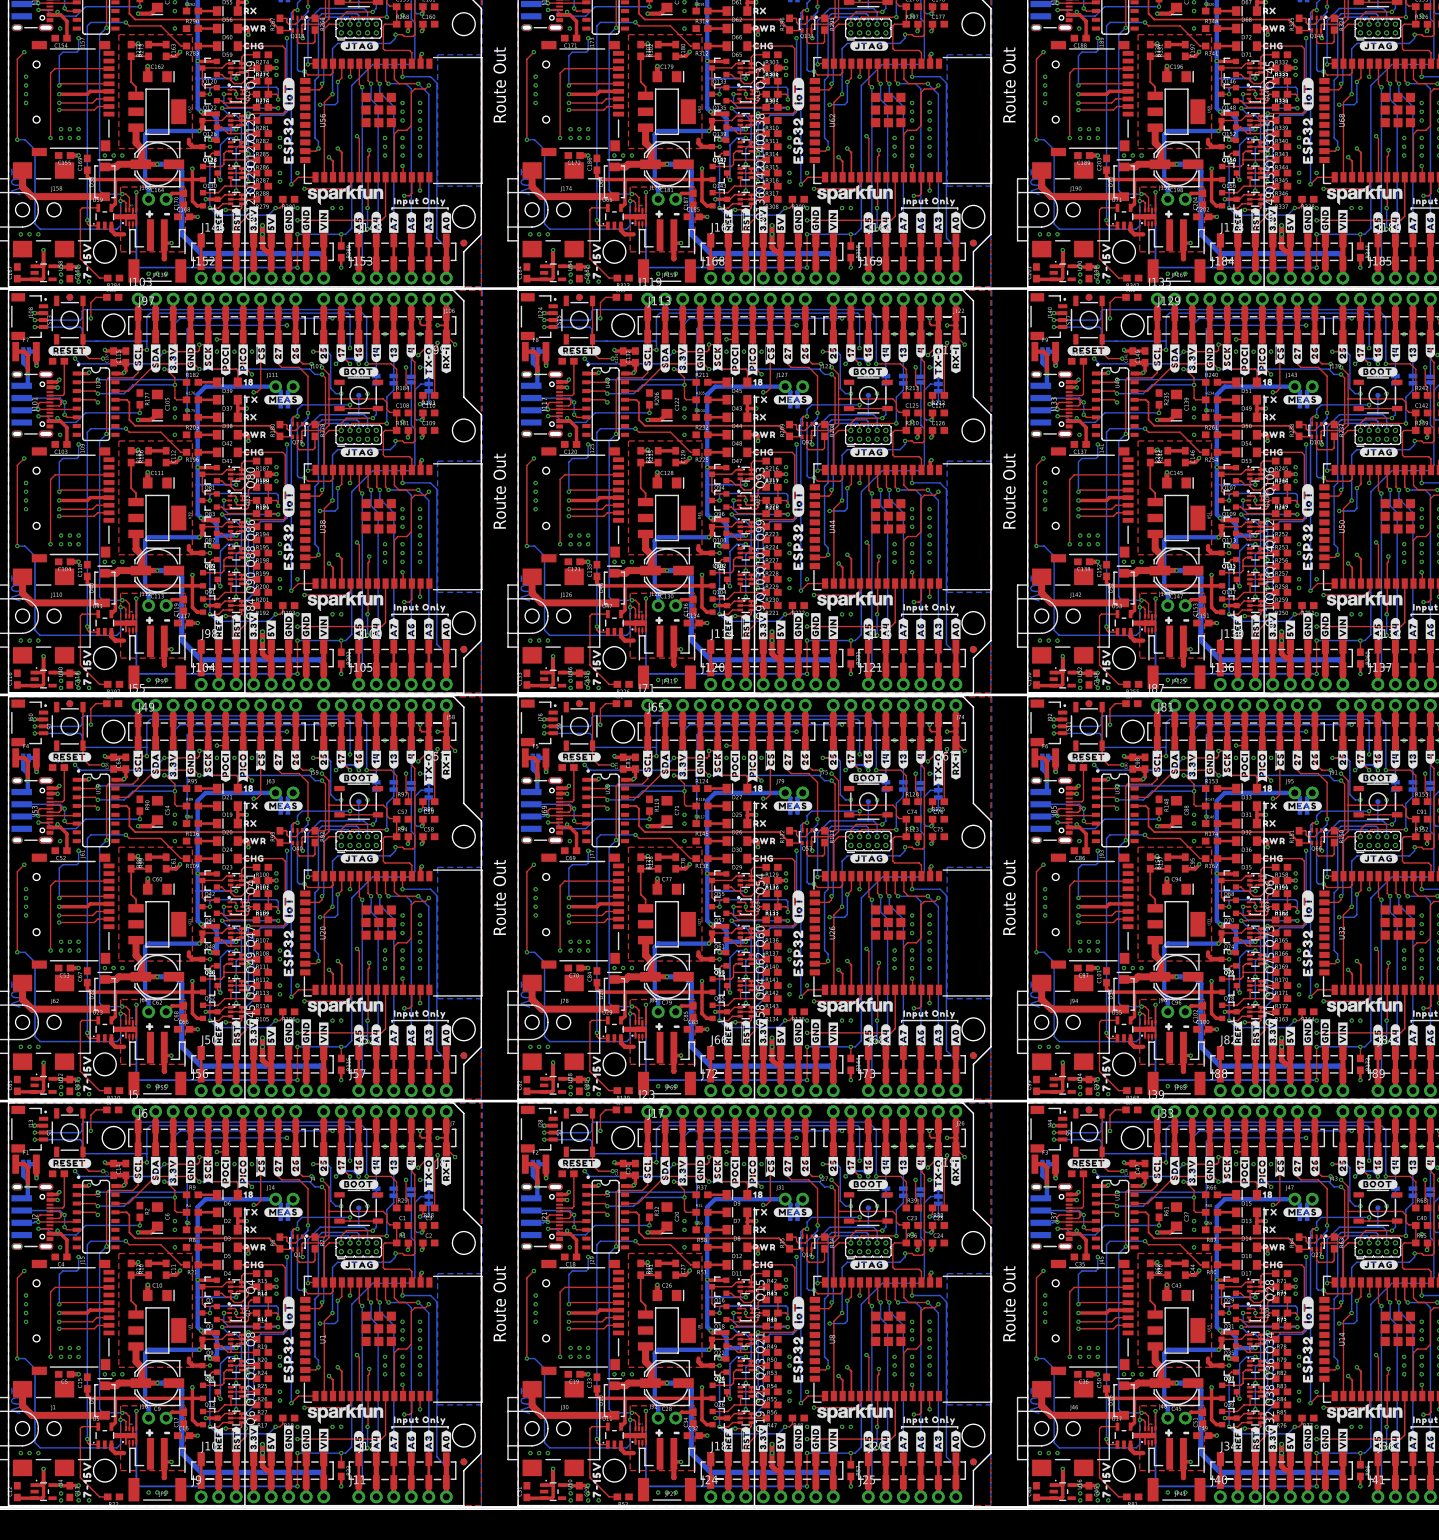
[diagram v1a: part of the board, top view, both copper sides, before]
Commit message: Fixed silkscreen and via interference on bottom layer;
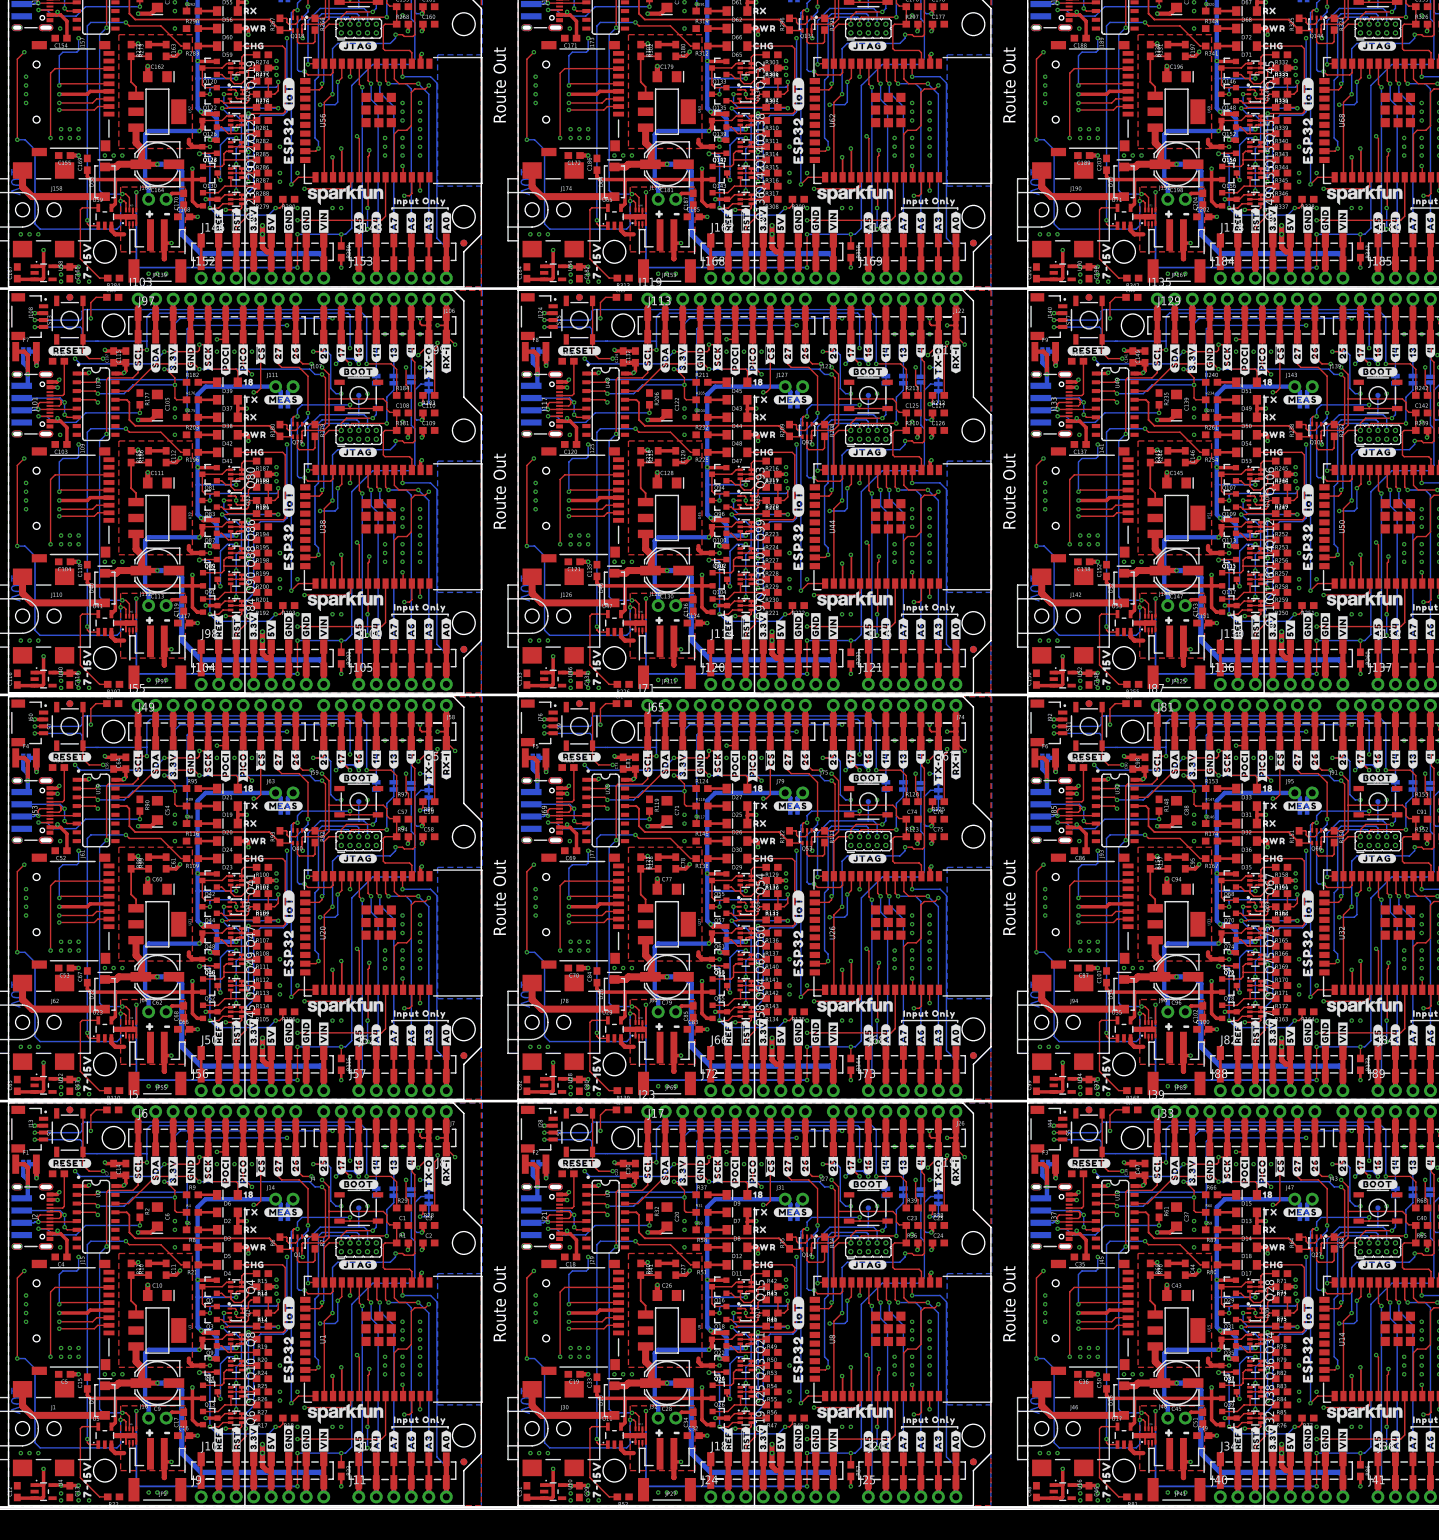
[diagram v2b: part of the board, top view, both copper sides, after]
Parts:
- moved U$1000 0.51 mm to (34.3, 195.3)
- moved U$1100 0.51 mm to (108.2, 195.3)
- moved U$1200 0.51 mm to (182.1, 195.3)
- moved U$700 0.51 mm to (34.3, 136.4)
- moved U$800 0.51 mm to (108.2, 136.4)
- moved U$900 0.51 mm to (182.1, 136.4)
- moved U$103 0.51 mm to (34.3, 18.5)
- moved U$200 0.51 mm to (108.2, 18.5)
- moved U$300 0.51 mm to (182.1, 18.5)
- moved U$400 0.51 mm to (34.3, 77.5)
- moved U$500 0.51 mm to (108.2, 77.5)
- moved U$600 0.51 mm to (182.1, 77.5)
- moved U$645 0.25 mm to (50.7, 152.8)
- moved U$745 0.25 mm to (124.6, 152.8)
- moved U$845 0.25 mm to (198.5, 152.8)
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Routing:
- net N$274: track 24.5 -> 27.5 mm
- net N$196: track 24.5 -> 27.5 mm
- net N$118: track 24.5 -> 27.5 mm
- net N$92: track 24.5 -> 27.5 mm
- net N$40: track 24.5 -> 27.5 mm
- net N$248: track 24.5 -> 27.5 mm
- net N$170: track 24.5 -> 27.5 mm
- net N$10: track 24.5 -> 27.5 mm
- net N$300: track 24.5 -> 27.5 mm
- net N$222: track 24.5 -> 27.5 mm
- net N$66: track 24.5 -> 27.5 mm
- net N$144: track 24.5 -> 27.5 mm
- net 5V9: track 97.3 -> 94.9 mm
- net 5V7: track 97.3 -> 94.9 mm
- net 5V6: track 97.3 -> 94.9 mm
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
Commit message: Updated design per Engineering checklist.
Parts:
- moved U$1027 0.76 mm to (125.3, 211.7)
- moved U$1045 0.76 mm to (125.3, 211.7)
- moved U$1127 0.76 mm to (199.3, 211.7)
- moved U$1145 0.76 mm to (199.3, 211.7)
- moved U$127 0.76 mm to (125.3, 34.9)
- moved U$145 0.76 mm to (125.3, 34.9)
- moved U$227 0.76 mm to (199.3, 34.9)
- moved U$245 0.76 mm to (199.3, 34.9)
- moved U$28 0.76 mm to (51.4, 34.9)
- moved U$327 0.76 mm to (51.4, 93.9)
- moved U$345 0.76 mm to (51.4, 93.9)
- moved U$427 0.76 mm to (125.3, 93.9)
- moved U$445 0.76 mm to (125.3, 93.9)
- moved U$46 0.76 mm to (51.4, 34.9)
- moved U$527 0.76 mm to (199.3, 93.9)
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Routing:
- net ESP32_GPIO14_TMS4: track 19.0 -> 20.8 mm
- net ESP32_GPIO14_TMS1: track 19.0 -> 20.8 mm
- net ESP32_GPIO14_TMS7: track 19.0 -> 20.8 mm
- net ESP32_GPIO14_TMS10: track 19.0 -> 20.8 mm
- net ESP32_GPIO14_TMS: track 19.0 -> 20.8 mm
- net ESP32_GPIO14_TMS3: track 19.0 -> 20.8 mm
- net ESP32_GPIO14_TMS9: track 19.0 -> 20.8 mm
- net ESP32_GPIO14_TMS6: track 19.0 -> 20.8 mm
- net ESP32_GPIO14_TMS2: track 19.0 -> 20.8 mm
- net ESP32_GPIO14_TMS5: track 19.0 -> 20.8 mm
- net ESP32_GPIO14_TMS8: track 19.0 -> 20.8 mm
- net ESP32_GPIO14_TMS11: track 19.0 -> 20.8 mm
- net ESP32_EN9: track 125.4 -> 123.8 mm
- net ESP32_EN8: track 125.4 -> 123.8 mm
- net ESP32_EN7: track 125.4 -> 123.8 mm
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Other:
- board text added: "1"
- board text added: "2"
- board text added: "3"
- board text added: "4"
